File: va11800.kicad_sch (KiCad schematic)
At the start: 253 parts, among them J1 Conn_01x16_Female, J3 Conn_01x16_Female, j2 MX-NoLED, k1 MX-NoLED, m1 MX-NoLED, p1 MX-NoLED, q1 MX-NoLED, t1 MX-NoLED, u1 MX-NoLED, x1 MX-NoLED, y1 MX-NoLED

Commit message: correct traces and mounting holes
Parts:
- D1, D10, D100, D101, D102, D103, D104, D105, D106, D107, D108, D109, D11, D110, D111, D112, D113, D114, D12, D13, D14, D15, D16, D17, D18, D19, D2, D20, D21, D22, D23, D25, D26, D27, D28, D29, D3, D30, D31, D32, D33, D34, D35, D36, D37, D38, D39, D4, D40, D41, D42, D43, D44, D45, D46, D47, D48, D49, D5, D50, D51, D52, D53, D54, D55, D56, D57, D58, D59, D6, D60, D61, D62, D63, D64, D65, D66, D67, D68, D69, D7, D70, D71, D72, D73, D74, D75, D76, D77, D78, D79, D8, D80, D81, D82, D83, D84, D86, D87, D88, D89, D9, D91, D93, D94, D95, D96, D97, D98, D99: footprint vuckale:Diode -> keebio:Diode-dual

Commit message: fix encoder placement and add 6u spacebar support
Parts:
- added D115: D_Small, keebio:Diode-dual, symbol Device:D_Small
- added R5, R6: R_Small, keebio:Resistor-Hybrid, symbol Device:R_Small
- added ResetSwitch1, ResetSwitch2: RESET, Button_Switch_SMD:SW_SPST_TL3342, symbol Switch:SW_DIP_x01
- added RmodX1: MX-NoLED, MX_Only:MXOnly-1U-NoLED, symbol MX_Alps_Hybrid:MX-NoLED
- added SW1, SW2, SW3, SW4, SW5: RotaryEncoder_Switch, keebio:RotaryEncoder_EC11, symbol Device:RotaryEncoder_Switch
- added space4: MX-NoLED, MX_Only:MXOnly-6U-NoSwitch, symbol MX_Alps_Hybrid:MX-NoLED
- D1, D10, D100, D101, D102, D103, D104, D105, D106, D107, D108, D109, D11, D110, D111, D112, D113, D114, D12, D13, D14, D15, D16, D17, D18, D19, D2, D20, D21, D22, D23, D25, D26, D27, D28, D29, D3, D30, D31, D32, D33, D34, D35, D36, D37, D38, D39, D4, D40, D41, D42, D43, D44, D45, D46, D47, D48, D49, D5, D50, D51, D52, D53, D54, D55, D56, D57, D58, D59, D6, D60, D61, D62, D63, D64, D65, D66, D67, D68, D69, D7, D70, D71, D72, D73, D74, D75, D76, D77, D78, D79, D8, D80, D81, D82, D83, D84, D86, D87, D88, D89, D9, D91, D93, D94, D95, D96, D97, D98, D99: LCSC (none) -> C77978
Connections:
- net GND: now also ResetSwitch1.2, ResetSwitch2.2, SW1.C, SW2.C, SW3.C, SW4.C, SW5.C
- net col0: now also SW4.S1
- net col6: now also RmodX1.1 (COL), SW2.S1, SW5.S2
- net col7: now also SW3.S1
- net col8: now also SW1.S1
- net row12: now also D115.1 (K)
- net at D83.2 (A), pause1.2 (ROW): now also SW2.S2
- net at D109.2 (A), kp_-1.2 (ROW): now also SW1.S2
- net en-row11: now reaches D80.2 (A), kp_enter1.2 (ROW)
- net en-row11: now also SW5.S1
- net at D5.2 (A), grave1.2 (ROW): now also SW4.S2
- net RST: now reaches J1.2 (Pin_2)
- net RST: now also ResetSwitch1.1, ResetSwitch2.1
- net en3-row5: now reaches D91.2 (A), backspace3.2 (ROW)
- net en3-row5: now also SW3.S2
- net A: now reaches J3.14 (Pin_14)
- net A: now also SW1.A, SW2.A, SW3.A, SW4.A, SW5.A
- net B: now reaches J3.15 (Pin_15)
- net B: now also SW1.B, SW5.B
- net B2: now reaches J3.16 (Pin_16)
- net B2: now also R5.2, R6.2
- new net: D115.2 (A), RmodX1.2 (ROW)
- new net B2R1: R5.1, SW3.B, SW4.B
- new net B2R2: R6.1, SW2.B
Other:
- moved on the sheet: D85, D90, D92, H1, H2, H3, H4, H5, J1, J3, R2, R3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

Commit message: cleanup traces
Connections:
- net A: now also J3.15 (Pin_15); no longer J3.14 (Pin_14)
- net B: now also J3.16 (Pin_16); no longer J3.15 (Pin_15)
- net B2: now also J3.14 (Pin_14); no longer J3.16 (Pin_16)
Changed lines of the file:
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@@
     )
   )
-  (global_label "B" (shape input) (at 343.408 137.414 270) (fields_autoplaced)
-    (effects (font (size 1.27 1.27)) (justify right))
-    (property "Intersheet References" "${INTERSHEET_REFS}" (id 0) (at 343.3286 141.0082 90)
+  (global_label "B" (shape input) (at 345.948 137.414 270) (fields_autoplaced)
+    (effects (font (size 1.27 1.27)) (justify right))
+    (property "Intersheet References" "${INTERSHEET_REFS}" (id 0) (at 345.8686 141.0082 90)
       (effects (font (size 1.27 1.27)) (justify right) hide)
     )
@@
     )
   )
-  (global_label "A" (shape input) (at 340.868 137.414 270) (fields_autoplaced)
-    (effects (font (size 1.27 1.27)) (justify right))
-    (property "Intersheet References" "${INTERSHEET_REFS}" (id 0) (at 340.7886 140.8268 90)
+  (global_label "A" (shape input) (at 343.408 137.414 270) (fields_autoplaced)
+    (effects (font (size 1.27 1.27)) (justify right))
+    (property "Intersheet References" "${INTERSHEET_REFS}" (id 0) (at 343.3286 140.8268 90)
       (effects (font (size 1.27 1.27)) (justify right) hide)
     )
@@
     )
   )
-  (global_label "B2" (shape input) (at 345.948 137.414 270) (fields_autoplaced)
-    (effects (font (size 1.27 1.27)) (justify right))
-    (property "Intersheet References" "${INTERSHEET_REFS}" (id 0) (at 345.8686 142.2177 90)
-      (effects (font (size 1.27 1.27)) (justify right) hide)
-    )
+  (global_label "B2" (shape input) (at 340.868 137.414 270) (fields_autoplaced)
+    (effects (font (size 1.27 1.27)) (justify right))
+    (property "Intersheet References" "${INTERSHEET_REFS}" (id 0) (at 340.7886 142.2177 90)
+      (effects (font (size 1.27 1.27)) (justify right) hide)
+    )

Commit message: fix ground for encoder and reset switch and trace cleanup
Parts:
- f1, f2, f3: footprint MX_Only:MXOnly-1U-NoLED -> MX_Only:MXOnly-1U
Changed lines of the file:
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@@
       (effects (font (size 0.508 0.508)))
     )
-    (property "Footprint" "MX_Only:MXOnly-1U-NoLED" (id 2) (at 236.855 206.375 0)
+    (property "Footprint" "MX_Only:MXOnly-1U" (id 2) (at 236.855 206.375 0)
       (effects (font (size 1.524 1.524)) hide)
     )
@@
       (effects (font (size 0.508 0.508)))
     )
-    (property "Footprint" "MX_Only:MXOnly-1U-NoLED" (id 2) (at 248.285 206.375 0)
+    (property "Footprint" "MX_Only:MXOnly-1U" (id 2) (at 248.285 206.375 0)
       (effects (font (size 1.524 1.524)) hide)
     )
@@
       (effects (font (size 0.508 0.508)))
     )
-    (property "Footprint" "MX_Only:MXOnly-1U-NoLED" (id 2) (at 236.855 226.695 0)
+    (property "Footprint" "MX_Only:MXOnly-1U" (id 2) (at 236.855 226.695 0)
       (effects (font (size 1.524 1.524)) hide)
     )
@@
     )
     (path "/00000000-0000-0000-0000-000061c1d772"
-      (reference "f1") (unit 1) (value "MX-NoLED") (footprint "MX_Only:MXOnly-1U-NoLED")
+      (reference "f1") (unit 1) (value "MX-NoLED") (footprint "MX_Only:MXOnly-1U")
     )
     (path "/00000000-0000-0000-0000-000061c2de20"
-      (reference "f2") (unit 1) (value "MX-NoLED") (footprint "MX_Only:MXOnly-1U-NoLED")
+      (reference "f2") (unit 1) (value "MX-NoLED") (footprint "MX_Only:MXOnly-1U")
     )
     (path "/00000000-0000-0000-0000-000061c1e3d6"
-      (reference "f3") (unit 1) (value "MX-NoLED") (footprint "MX_Only:MXOnly-1U-NoLED")
+      (reference "f3") (unit 1) (value "MX-NoLED") (footprint "MX_Only:MXOnly-1U")
     )
     (path "/00000000-0000-0000-0000-000061c2de2e"

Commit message: cleanup kicad_sch
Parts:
- removed space4: MX-NoLED, MX_Only:MXOnly-6U-NoSwitch, symbol MX_Alps_Hybrid:MX-NoLED
- f1, f2, f3: footprint MX_Only:MXOnly-1U -> MX_Only:MXOnly-1U-NoLED
- renumbered D85 to D1, D7 to D10, D8 to D11, D9 to D12, D10 to D13, D11 to D14, D12 to D15, D13 to D16, D14 to D17, D15 to D18, D16 to D19, D90 to D2, D17 to D20, D18 to D21, D19 to D22, D20 to D23, D21 to D24, D22 to D25, D23 to D26, D25 to D27, D26 to D28, D27 to D29, D92 to D3, D28 to D30, D29 to D31, D30 to D32, D31 to D33, D32 to D34, D33 to D35, D34 to D36, D35 to D37, D36 to D38, D37 to D39, D1 to D4, D38 to D40, D39 to D41, D40 to D42, D41 to D43, D42 to D44, D43 to D45, D44 to D46, D45 to D47, D46 to D48, D47 to D49, D2 to D5, D48 to D50, D49 to D51, D50 to D52, D51 to D53, D52 to D54, D53 to D55, D54 to D56, D55 to D57, D56 to D58, D57 to D59, D3 to D6, D58 to D60, D59 to D61, D60 to D62, D61 to D63, D62 to D64, D63 to D65, D64 to D66, D65 to D67, D66 to D68, D67 to D69, D4 to D7, D68 to D70, D69 to D71, D75 to D72, D70 to D73, D71 to D74, D72 to D75, D73 to D76, D74 to D77, D80 to D78, D76 to D79, D5 to D8, D77 to D80, D78 to D81, D79 to D82, D81 to D83, D82 to D84, D115 to D85, D83 to D86, D84 to D87, D86 to D88, D87 to D89, D6 to D9, D88 to D90, D89 to D91, D93 to D92, D94 to D93, D95 to D94, D91 to D95, J3 to J2, R2 to R1, R3 to R2, R4 to R3, R5 to R4, R6 to R5, SW4 to encA1, SW3 to encA2, SW2 to encB1, SW1 to encC1, SW5 to encC2, d24 to key_d1, h6 to key_h1, j2 to key_j1, r1 to key_r1, space1 to space2, space2 to space3, space3 to space4
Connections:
- net col4: no longer down1.1 (COL)
- net row12: now also D27.1 (K)
- net row13: no longer D27.1 (K)
- net encB_row1_d: now reaches D86.2 (A), encB1.S2, pause1.2 (ROW)
- net encC1_row0_d: now reaches D109.2 (A), encC1.S2, kp_-1.2 (ROW)
- net encA1_row5_d: now reaches D8.2 (A), encA1.S2, grave1.2 (ROW)
- net at D64.2 (A): no longer down1.2 (ROW)
- net B2R1 renamed encA_R
- net B2R2 renamed encB_R
- net en-row11 renamed encC2_row11_d
- net en3-row5 renamed encA2_row5_d
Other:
- moved on the sheet: D1, D100, D101, D102, D103, D104, D105, D106, D107, D109, D110, D111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

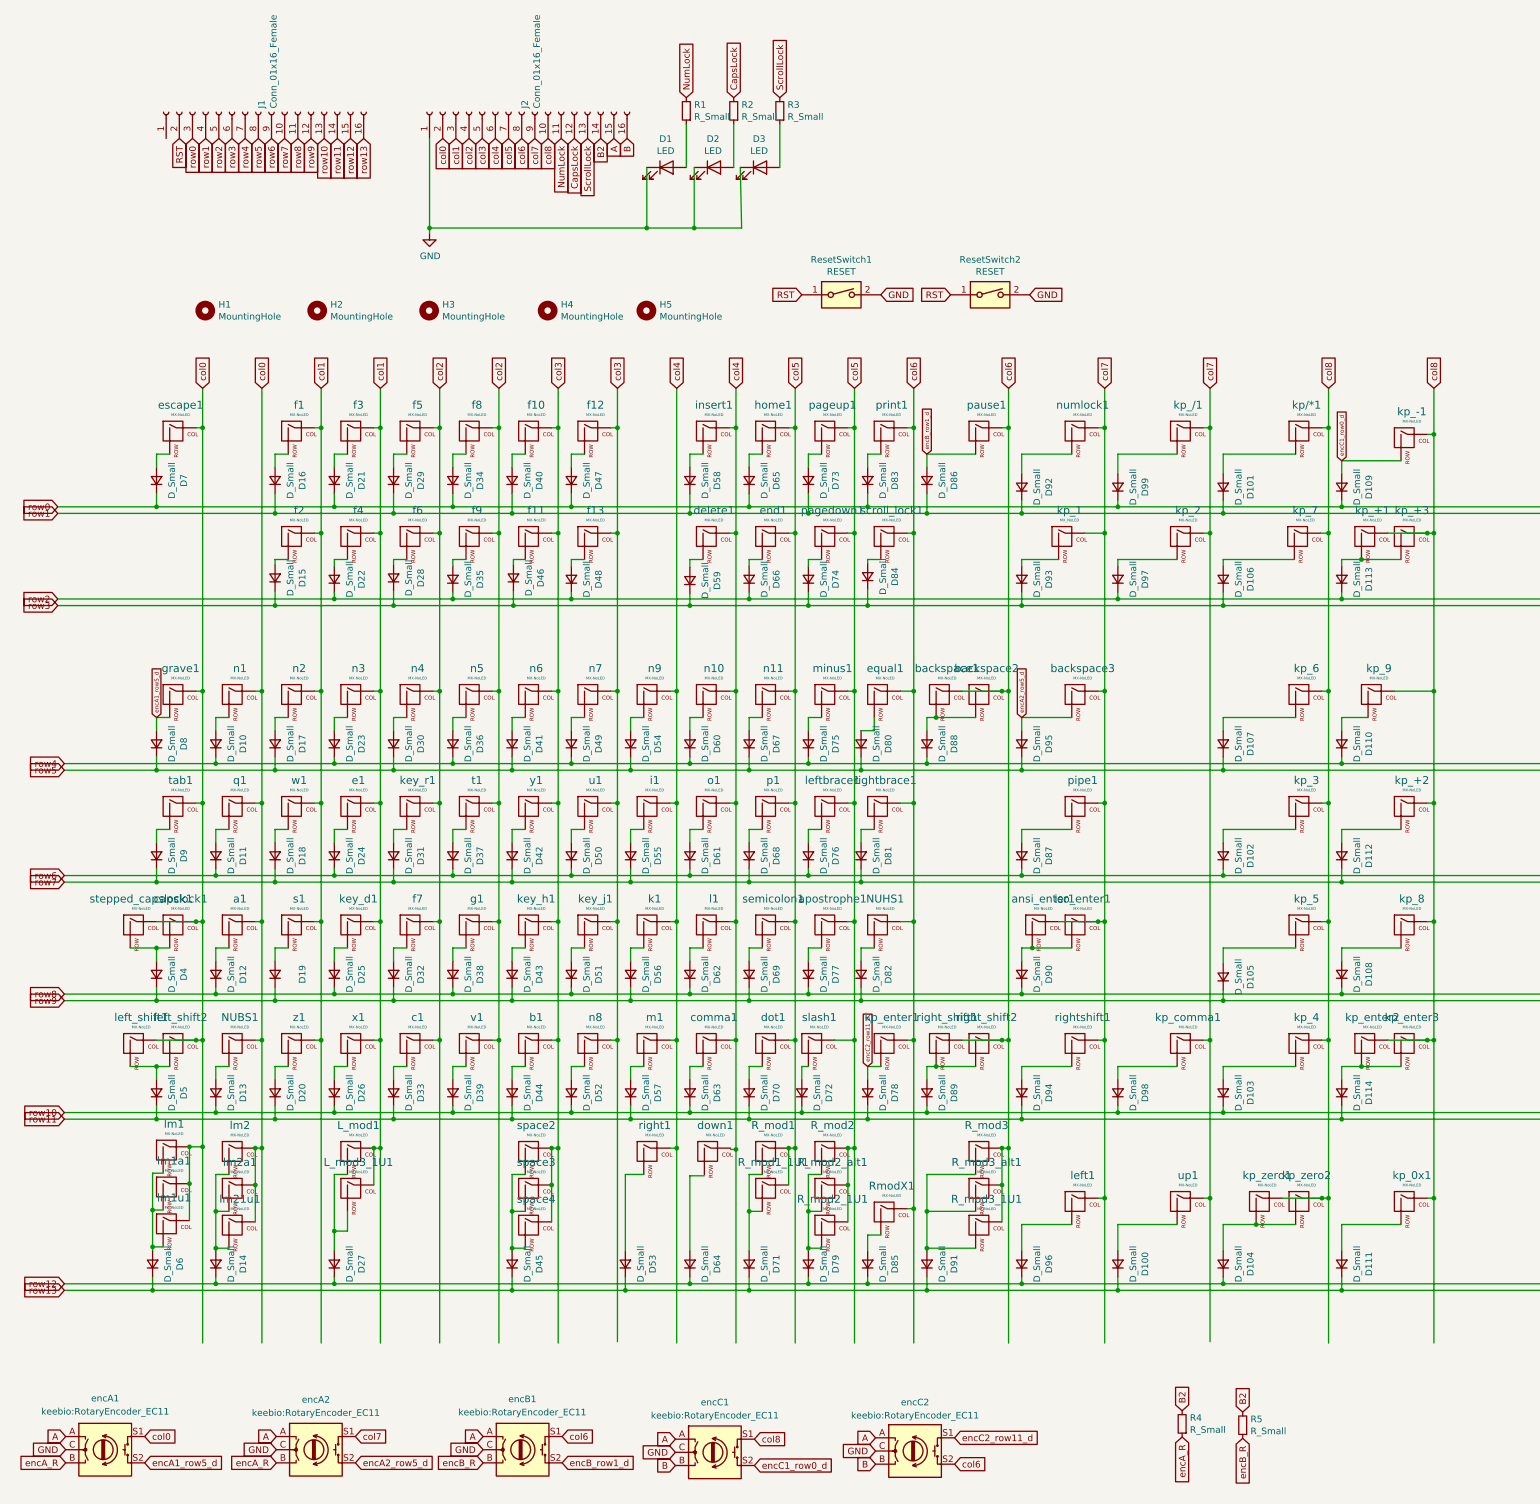
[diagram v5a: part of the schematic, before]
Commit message: rename symbols in .kicad_sch
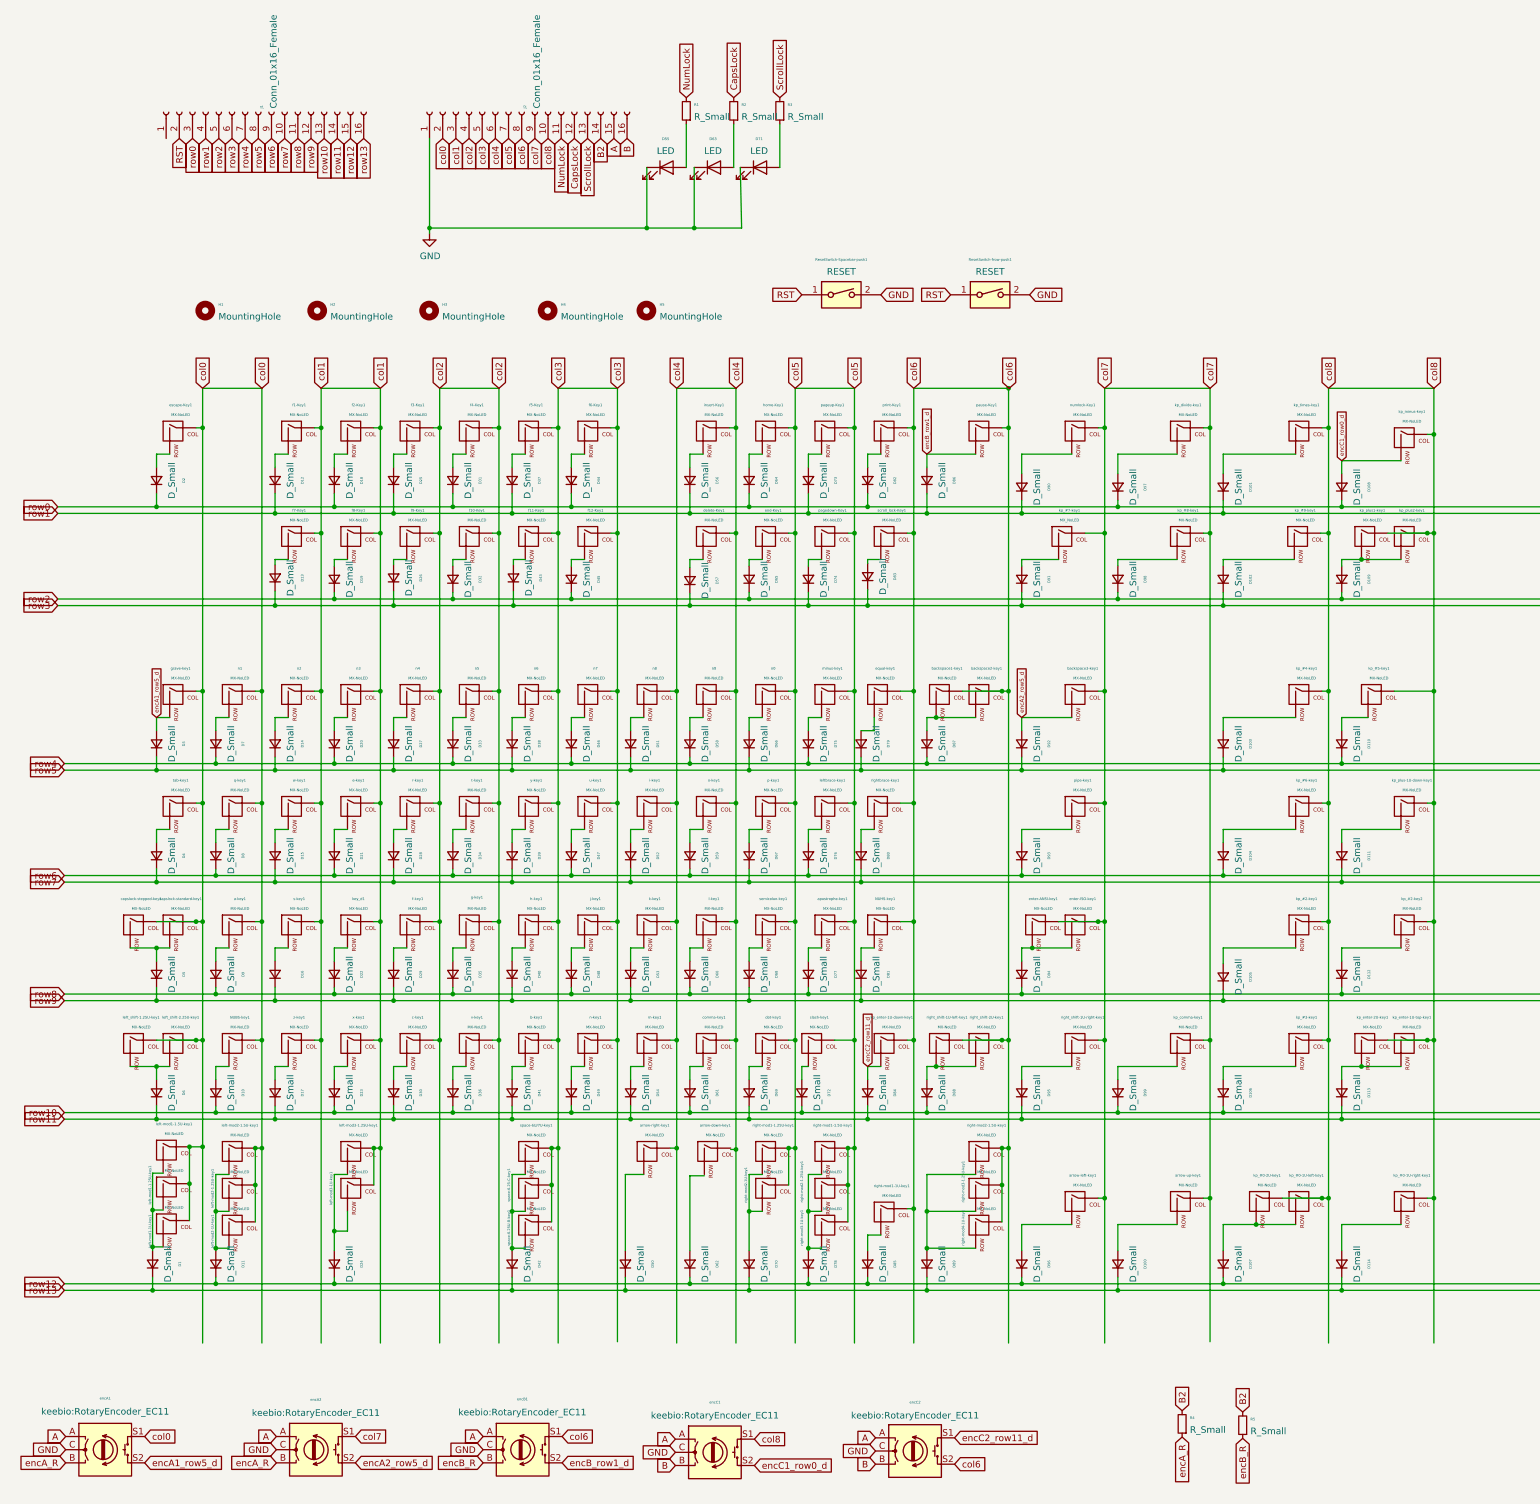
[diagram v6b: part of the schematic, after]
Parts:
- NUBS-key1: renamed from NUBS1; footprint MX_Only:MXOnly-1U-NoLED -> ai03:MXOnly-1U-NoLED
- NUHS-key1: renamed from NUHS1; footprint MX_Only:MXOnly-1U-NoLED -> ai03:MXOnly-1U-NoLED
- a-key1: renamed from a1; footprint MX_Only:MXOnly-1U-NoLED -> ai03:MXOnly-1U-NoLED
- apostrophe-key1: renamed from apostrophe1; footprint MX_Only:MXOnly-1U-NoLED -> ai03:MXOnly-1U-NoLED
- arrow-down-key1: renamed from down1; footprint MX_Only:MXOnly-1U-NoLED -> ai03:MXOnly-1U-NoLED
- arrow-left-key1: renamed from left1; footprint MX_Only:MXOnly-1U-NoLED -> ai03:MXOnly-1U-NoLED
- arrow-right-key1: renamed from right1; footprint MX_Only:MXOnly-1U-NoLED -> ai03:MXOnly-1U-NoLED
- arrow-up-key1: renamed from up1; footprint MX_Only:MXOnly-1U-NoLED -> ai03:MXOnly-1U-NoLED
- b-key1: renamed from b1; footprint MX_Only:MXOnly-1U-NoLED -> ai03:MXOnly-1U-NoLED
- backspace1-key1: renamed from backspace1; footprint MX_Only:MXOnly-1U-NoLED -> ai03:MXOnly-1U-NoLED
- backspace2-key1: renamed from backspace2; footprint MX_Only:MXOnly-2U-ReversedStabilizers-NoLED -> ai03:MXOnly-2U-ReversedStabilizers-NoLED
- backspace3-key1: renamed from backspace3; footprint MX_Only:MXOnly-1U-NoLED -> ai03:MXOnly-1U-NoLED
- c-key1: renamed from c1; footprint MX_Only:MXOnly-1U-NoLED -> ai03:MXOnly-1U-NoLED
- capslock-standard-key1: renamed from capslock1; footprint MX_Only:MXOnly-1.75U-NoLED -> ai03:MXOnly-1.75U-NoLED
- capslock-stepped-key1: renamed from stepped_capslock1; footprint MX_Only:MXOnly-1.25U-NoLED -> ai03:MXOnly-1.25U-NoLED
- comma-key1: renamed from comma1; footprint MX_Only:MXOnly-1U-NoLED -> ai03:MXOnly-1U-NoLED
- delete-Key1: renamed from delete1; footprint MX_Only:MXOnly-1U-NoLED -> ai03:MXOnly-1U-NoLED
- dot-key1: renamed from dot1; footprint MX_Only:MXOnly-1U-NoLED -> ai03:MXOnly-1U-NoLED
- e-key1: renamed from e1; footprint MX_Only:MXOnly-1U-NoLED -> ai03:MXOnly-1U-NoLED
- end-Key1: renamed from end1; footprint MX_Only:MXOnly-1U-NoLED -> ai03:MXOnly-1U-NoLED
- enter-ANSI-key1: renamed from ansi_enter1; footprint MX_Only:MXOnly-2.25U-NoLED -> ai03:MXOnly-2.25U-NoLED
- enter-ISO-key1: renamed from iso_enter1; footprint MX_Only:MXOnly-ISO-ReversedStabilizers-NoLED -> ai03:MXOnly-ISO-ReversedStabilizers-NoLED
- equal-key1: renamed from equal1; footprint MX_Only:MXOnly-1U-NoLED -> ai03:MXOnly-1U-NoLED
- escape-Key1: renamed from escape1; footprint MX_Only:MXOnly-1U-NoLED -> ai03:MXOnly-1U-NoLED
- f-key1: renamed from f7; footprint MX_Only:MXOnly-1U-NoLED -> ai03:MXOnly-1U-NoLED
- f1-Key1: renamed from f1; footprint MX_Only:MXOnly-1U-NoLED -> ai03:MXOnly-1U-NoLED
- f10-Key1: renamed from f9; footprint MX_Only:MXOnly-1U-NoLED -> ai03:MXOnly-1U-NoLED
- f11-Key1: renamed from f11; footprint MX_Only:MXOnly-1U-NoLED -> ai03:MXOnly-1U-NoLED
- f12-Key1: renamed from f13; footprint MX_Only:MXOnly-1U-NoLED -> ai03:MXOnly-1U-NoLED
- f2-Key1: renamed from f3; footprint MX_Only:MXOnly-1U-NoLED -> ai03:MXOnly-1U-NoLED
- f3-Key1: renamed from f5; footprint MX_Only:MXOnly-1U-NoLED -> ai03:MXOnly-1U-NoLED
- f4-Key1: renamed from f8; footprint MX_Only:MXOnly-1U-NoLED -> ai03:MXOnly-1U-NoLED
- f5-Key1: renamed from f10; footprint MX_Only:MXOnly-1U-NoLED -> ai03:MXOnly-1U-NoLED
- f6-Key1: renamed from f12; footprint MX_Only:MXOnly-1U-NoLED -> ai03:MXOnly-1U-NoLED
- f7-Key1: renamed from f2; footprint MX_Only:MXOnly-1U-NoLED -> ai03:MXOnly-1U-NoLED
- f8-Key1: renamed from f4; footprint MX_Only:MXOnly-1U-NoLED -> ai03:MXOnly-1U-NoLED
- f9-Key1: renamed from f6; footprint MX_Only:MXOnly-1U-NoLED -> ai03:MXOnly-1U-NoLED
- g-key1: renamed from g1; footprint MX_Only:MXOnly-1U-NoLED -> ai03:MXOnly-1U-NoLED
- grave-key1: renamed from grave1; footprint MX_Only:MXOnly-1U-NoLED -> ai03:MXOnly-1U-NoLED
- h-key1: renamed from key_h1; footprint MX_Only:MXOnly-1U-NoLED -> ai03:MXOnly-1U-NoLED
- home-Key1: renamed from home1; footprint MX_Only:MXOnly-1U-NoLED -> ai03:MXOnly-1U-NoLED
- i-key1: renamed from i1; footprint MX_Only:MXOnly-1U-NoLED -> ai03:MXOnly-1U-NoLED
- insert-Key1: renamed from insert1; footprint MX_Only:MXOnly-1U-NoLED -> ai03:MXOnly-1U-NoLED
- j-key1: renamed from key_j1; footprint MX_Only:MXOnly-1U-NoLED -> ai03:MXOnly-1U-NoLED
- k-key1: renamed from k1; footprint MX_Only:MXOnly-1U-NoLED -> ai03:MXOnly-1U-NoLED
- key_d1, n1, n2, n3, n4, n5, n6, n7: footprint MX_Only:MXOnly-1U-NoLED -> ai03:MXOnly-1U-NoLED
- kp_#0-1U-left-key1: renamed from kp_zero2; footprint MX_Only:MXOnly-1U-NoLED -> ai03:MXOnly-1U-NoLED
- kp_#0-1U-right-key1: renamed from kp_0x1; footprint MX_Only:MXOnly-1U-NoLED -> ai03:MXOnly-1U-NoLED
- kp_#0-2U-key1: renamed from kp_zero1; footprint MX_Only:MXOnly-2U-ReversedStabilizers-NoLED -> ai03:MXOnly-2U-ReversedStabilizers-NoLED
- kp_#2-key1: renamed from kp_5; footprint MX_Only:MXOnly-1U-NoLED -> ai03:MXOnly-1U-NoLED
- kp_#2-key2: renamed from kp_8; footprint MX_Only:MXOnly-1U-NoLED -> ai03:MXOnly-1U-NoLED
- kp_#3-key1: renamed from kp_4; footprint MX_Only:MXOnly-1U-NoLED -> ai03:MXOnly-1U-NoLED
- kp_#4-key1: renamed from kp_6; footprint MX_Only:MXOnly-1U-NoLED -> ai03:MXOnly-1U-NoLED
- kp_#5-key1: renamed from kp_9; footprint MX_Only:MXOnly-1U-NoLED -> ai03:MXOnly-1U-NoLED
- kp_#6-key1: renamed from kp_3; footprint MX_Only:MXOnly-1U-NoLED -> ai03:MXOnly-1U-NoLED
- kp_#7-key1: renamed from kp_1; footprint MX_Only:MXOnly-1U-NoLED -> ai03:MXOnly-1U-NoLED
- kp_#8-key1: renamed from kp_2; footprint MX_Only:MXOnly-1U-NoLED -> ai03:MXOnly-1U-NoLED
- kp_#9-key1: renamed from kp_7; footprint MX_Only:MXOnly-1U-NoLED -> ai03:MXOnly-1U-NoLED
- kp_comma-key1: renamed from kp_comma1; footprint MX_Only:MXOnly-1U-NoLED -> ai03:MXOnly-1U-NoLED
- kp_divide-key1: renamed from kp_/1; footprint MX_Only:MXOnly-1U-NoLED -> ai03:MXOnly-1U-NoLED
- kp_enter-1U-down-key1: renamed from kp_enter1; footprint MX_Only:MXOnly-1U-NoLED -> ai03:MXOnly-1U-NoLED
- kp_enter-1U-top-key1: renamed from kp_enter3; footprint MX_Only:MXOnly-1U-NoLED -> ai03:MXOnly-1U-NoLED
- kp_enter-2U-key1: renamed from kp_enter2; footprint MX_Only:MXOnly-2U-VerticalStabilizers-NoLED -> ai03:MXOnly-2U-VerticalStabilizers-NoLED
- kp_minus-key1: renamed from kp_-1; footprint MX_Only:MXOnly-1U-NoLED -> ai03:MXOnly-1U-NoLED
- kp_plus-1U-down-key1: renamed from kp_+2; footprint MX_Only:MXOnly-1U-NoLED -> ai03:MXOnly-1U-NoLED
- kp_plus1-key1: renamed from kp_+1; footprint MX_Only:MXOnly-2U-VerticalStabilizers-NoLED -> ai03:MXOnly-2U-VerticalStabilizers-NoLED
- kp_plus2-key1: renamed from kp_+3; footprint MX_Only:MXOnly-1U-NoLED -> ai03:MXOnly-1U-NoLED
- kp_times-key1: renamed from kp/*1; footprint MX_Only:MXOnly-1U-NoLED -> ai03:MXOnly-1U-NoLED
- l-key1: renamed from l1; footprint MX_Only:MXOnly-1U-NoLED -> ai03:MXOnly-1U-NoLED
- left-mod1-1.25U-key1: renamed from lm1a1; footprint MX_Only:MXOnly-1.25U-NoLED -> ai03:MXOnly-1.25U-NoLED
- left-mod1-1.5U-key1: renamed from lm1; footprint MX_Only:MXOnly-1.5U-NoLED -> ai03:MXOnly-1.5U-NoLED
- left-mod1-1U-key1: renamed from lm1u1; footprint MX_Only:MXOnly-1U-NoLED -> ai03:MXOnly-1U-NoLED
- left-mod2-1.25U-key1: renamed from lm2a1; footprint MX_Only:MXOnly-1.25U-NoLED -> ai03:MXOnly-1.25U-NoLED
- left-mod2-1.5U-key1: renamed from lm2; footprint MX_Only:MXOnly-1.5U-NoLED -> ai03:MXOnly-1.5U-NoLED
- left-mod2-1U-key1: renamed from lm21u1; footprint MX_Only:MXOnly-1U-NoLED -> ai03:MXOnly-1U-NoLED
- left-mod3-1.25U-key1: renamed from L_mod1; footprint MX_Only:MXOnly-1.25U-NoLED -> ai03:MXOnly-1.25U-NoLED
- left-mod3-1U-key1: renamed from L_mod3_1U1; footprint MX_Only:MXOnly-1U-NoLED -> ai03:MXOnly-1U-NoLED
- left_shift-1.25U-key1: renamed from left_shift1; footprint MX_Only:MXOnly-1.25U-NoLED -> ai03:MXOnly-1.25U-NoLED
- left_shift-2.25U-key1: renamed from left_shift2; footprint MX_Only:MXOnly-2.25U-NoLED -> ai03:MXOnly-2.25U-NoLED
- leftbrace-key1: renamed from leftbrace1; footprint MX_Only:MXOnly-1U-NoLED -> ai03:MXOnly-1U-NoLED
- m-key1: renamed from m1; footprint MX_Only:MXOnly-1U-NoLED -> ai03:MXOnly-1U-NoLED
- minus-key1: renamed from minus1; footprint MX_Only:MXOnly-1U-NoLED -> ai03:MXOnly-1U-NoLED
- n-key1: renamed from n8; footprint MX_Only:MXOnly-1U-NoLED -> ai03:MXOnly-1U-NoLED
- n0: renamed from n11; footprint MX_Only:MXOnly-1U-NoLED -> ai03:MXOnly-1U-NoLED
- n8: renamed from n9; footprint MX_Only:MXOnly-1U-NoLED -> ai03:MXOnly-1U-NoLED
- n9: renamed from n10; footprint MX_Only:MXOnly-1U-NoLED -> ai03:MXOnly-1U-NoLED
- numlock-Key1: renamed from numlock1; footprint MX_Only:MXOnly-1U-NoLED -> ai03:MXOnly-1U-NoLED
- o-key1: renamed from o1; footprint MX_Only:MXOnly-1U-NoLED -> ai03:MXOnly-1U-NoLED
- p-key1: renamed from p1; footprint MX_Only:MXOnly-1U-NoLED -> ai03:MXOnly-1U-NoLED
- pagedown-Key1: renamed from pagedown1; footprint MX_Only:MXOnly-1U-NoLED -> ai03:MXOnly-1U-NoLED
- pageup-Key1: renamed from pageup1; footprint MX_Only:MXOnly-1U-NoLED -> ai03:MXOnly-1U-NoLED
- pause-Key1: renamed from pause1; footprint MX_Only:MXOnly-1U-NoLED -> ai03:MXOnly-1U-NoLED
- pipe-key1: renamed from pipe1; footprint MX_Only:MXOnly-1.5U-NoLED -> ai03:MXOnly-1.5U-NoLED
- print-Key1: renamed from print1; footprint MX_Only:MXOnly-1U-NoLED -> ai03:MXOnly-1U-NoLED
- q-key1: renamed from q1; footprint MX_Only:MXOnly-1U-NoLED -> ai03:MXOnly-1U-NoLED
- r-key1: renamed from key_r1; footprint MX_Only:MXOnly-1U-NoLED -> ai03:MXOnly-1U-NoLED
- right-mod1-1.25U-key1: renamed from R_mod1; footprint MX_Only:MXOnly-1.25U-NoLED -> ai03:MXOnly-1.25U-NoLED
- right-mod1-1.5U-key1: renamed from R_mod2; footprint MX_Only:MXOnly-1.5U-NoLED -> ai03:MXOnly-1.5U-NoLED
- right-mod1-1U-key1: renamed from RmodX1; footprint MX_Only:MXOnly-1U-NoLED -> ai03:MXOnly-1U-NoLED
- right-mod2-1.25U-key1: renamed from R_mod2_alt1; footprint MX_Only:MXOnly-1.25U-NoLED -> ai03:MXOnly-1.25U-NoLED
- right-mod2-1.5U-key1: renamed from R_mod3; footprint MX_Only:MXOnly-1.5U-NoLED -> ai03:MXOnly-1.5U-NoLED
- right-mod2-1U-key1: renamed from R_mod1_1U1; footprint MX_Only:MXOnly-1U-NoLED -> ai03:MXOnly-1U-NoLED
- right-mod3-1.25U-key1: renamed from R_mod3_alt1; footprint MX_Only:MXOnly-1.25U-NoLED -> ai03:MXOnly-1.25U-NoLED
- right-mod3-1U-key1: renamed from R_mod2_1U1; footprint MX_Only:MXOnly-1U-NoLED -> ai03:MXOnly-1U-NoLED
- right-mod4-1U-key1: renamed from R_mod3_1U1; footprint MX_Only:MXOnly-1U-NoLED -> ai03:MXOnly-1U-NoLED
- right_shift-1U-left-key1: renamed from right_shift1; footprint MX_Only:MXOnly-1U-NoLED -> ai03:MXOnly-1U-NoLED
- right_shift-1U-right-key1: renamed from rightshift1; footprint MX_Only:MXOnly-1U-NoLED -> ai03:MXOnly-1U-NoLED
- right_shift-2U-key1: renamed from right_shift2; footprint MX_Only:MXOnly-2U-NoLED -> ai03:MXOnly-2U-NoLED
- rightbrace-key1: renamed from rightbrace1; footprint MX_Only:MXOnly-1U-NoLED -> ai03:MXOnly-1U-NoLED
- s-key1: renamed from s1; footprint MX_Only:MXOnly-1U-NoLED -> ai03:MXOnly-1U-NoLED
- scroll_lock-Key1: renamed from scroll_lock1; footprint MX_Only:MXOnly-1U-NoLED -> ai03:MXOnly-1U-NoLED
- semicolon-key1: renamed from semicolon1; footprint MX_Only:MXOnly-1U-NoLED -> ai03:MXOnly-1U-NoLED
- slash-key1: renamed from slash1; footprint MX_Only:MXOnly-1U-NoLED -> ai03:MXOnly-1U-NoLED
- space-6.25-C-key1: renamed from space3; footprint MX_Only:MXOnly-6.25U-NoLED -> ai03:MXOnly-6.25U-NoLED
- space-6.25U-B-key1: renamed from space4; footprint MX_Only:MXOnly-6.25U-NoLED -> ai03:MXOnly-6.25U-NoLED
- space-6U/7U-key1: renamed from space2; footprint MX_Only:MXOnly-7U-NoLED -> ai03:MXOnly-7U-NoLED
- t-key1: renamed from t1; footprint MX_Only:MXOnly-1U-NoLED -> ai03:MXOnly-1U-NoLED
- tab-key1: renamed from tab1; footprint MX_Only:MXOnly-1.5U-NoLED -> ai03:MXOnly-1.5U-NoLED
- u-key1: renamed from u1; footprint MX_Only:MXOnly-1U-NoLED -> ai03:MXOnly-1U-NoLED
- v-key1: renamed from v1; footprint MX_Only:MXOnly-1U-NoLED -> ai03:MXOnly-1U-NoLED
- w-key1: renamed from w1; footprint MX_Only:MXOnly-1U-NoLED -> ai03:MXOnly-1U-NoLED
- x-key1: renamed from x1; footprint MX_Only:MXOnly-1U-NoLED -> ai03:MXOnly-1U-NoLED
- y-key1: renamed from y1; footprint MX_Only:MXOnly-1U-NoLED -> ai03:MXOnly-1U-NoLED
- z-key1: renamed from z1; footprint MX_Only:MXOnly-1U-NoLED -> ai03:MXOnly-1U-NoLED
- renumbered D6 to D1, D13 to D10, D106 to D102, D107 to D103, D102 to D104, D103 to D106, D104 to D107, D109 to D108, D113 to D109, D14 to D11, D112 to D111, D108 to D112, D114 to D113, D111 to D114, D16 to D12, D15 to D13, D17 to D14, D18 to D15, D19 to D16, D20 to D17, D21 to D18, D22 to D19, D7 to D2, D23 to D20, D24 to D21, D25 to D22, D26 to D23, D27 to D24, D29 to D25, D28 to D26, D30 to D27, D31 to D28, D32 to D29, D8 to D3, D33 to D30, D34 to D31, D35 to D32, D36 to D33, D37 to D34, D38 to D35, D39 to D36, D40 to D37, D41 to D38, D42 to D39, D9 to D4, D43 to D40, D44 to D41, D45 to D42, D46 to D43, D47 to D44, D48 to D45, D49 to D46, D50 to D47, D51 to D48, D52 to D49, D4 to D5, D53 to D50, D54 to D51, D55 to D52, D56 to D53, D57 to D54, D1 to D55, D58 to D56, D59 to D57, D60 to D58, D61 to D59, D5 to D6, D62 to D60, D63 to D61, D64 to D62, D2 to D63, D65 to D64, D66 to D65, D67 to D66, D68 to D67, D69 to D68, D70 to D69, D10 to D7, D71 to D70, D3 to D71, D79 to D78, D80 to D79, D11 to D8, D81 to D80, D82 to D81, D83 to D82, D84 to D83, D78 to D84, D88 to D87, D89 to D88, D91 to D89, D12 to D9, D92 to D90, D93 to D91, D95 to D92, D87 to D93, D90 to D94, D94 to D95, D99 to D97, D97 to D98, D98 to D99, ResetSwitch1 to ResetSwitch-Spacebar-push1, ResetSwitch2 to ResetSwitch-frow-push1

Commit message: fix excess traces on alpha keys
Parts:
- D1, D10, D100, D101, D102, D103, D104, D105, D106, D107, D108, D109, D11, D110, D111, D112, D113, D114, D12, D13, D14, D15, D16, D17, D18, D19, D2, D20, D21, D22, D23, D24, D25, D26, D27, D28, D29, D3, D30, D31, D32, D33, D34, D35, D36, D37, D38, D39, D4, D40, D41, D42, D43, D44, D45, D46, D47, D48, D49, D5, D50, D51, D52, D53, D54, D56, D57, D58, D59, D6, D60, D61, D62, D64, D65, D66, D67, D68, D69, D7, D70, D72, D73, D74, D75, D76, D77, D78, D79, D8, D80, D81, D82, D83, D84, D85, D86, D87, D88, D89, D9, D90, D91, D92, D93, D94, D95, D96, D97, D98, D99: LCSC C77978 -> C115103
